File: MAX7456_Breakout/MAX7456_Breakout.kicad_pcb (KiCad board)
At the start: 4 copper layers, 18.3 x 38.6 mm, 16 parts, among them J1 Conn_01x14_Socket, U1 MAX7456EUI_, Y1 27MHz

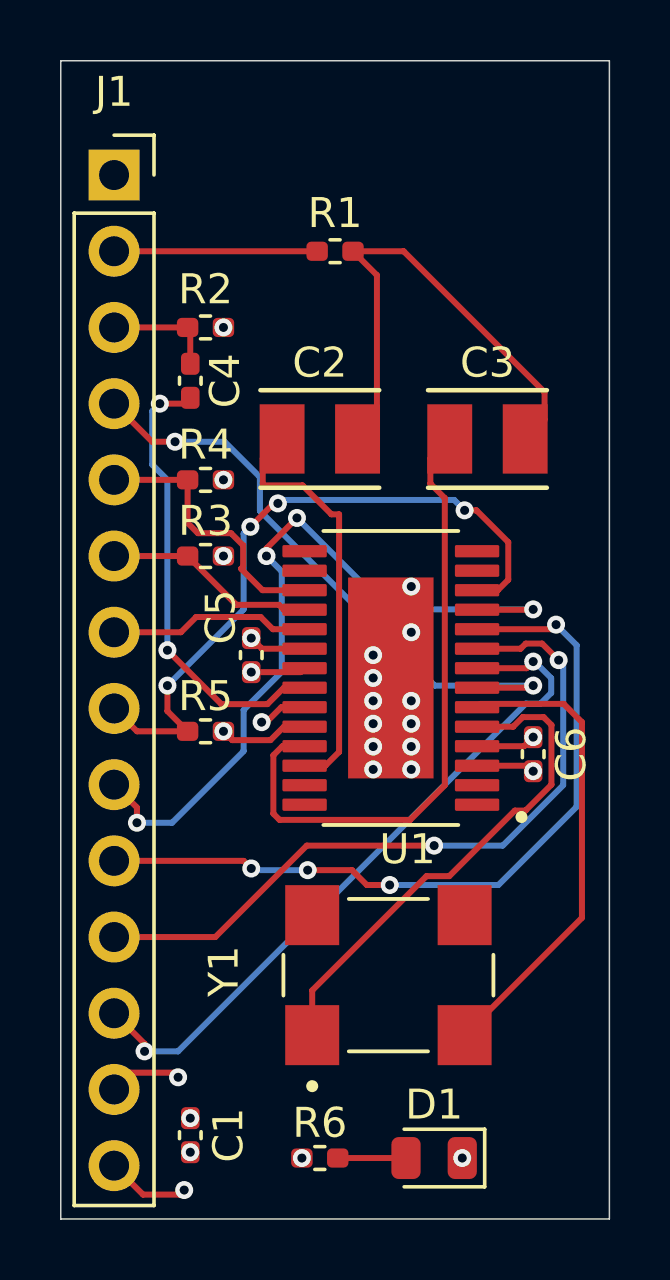
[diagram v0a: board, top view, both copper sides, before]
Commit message: Added 10k pullup on reset
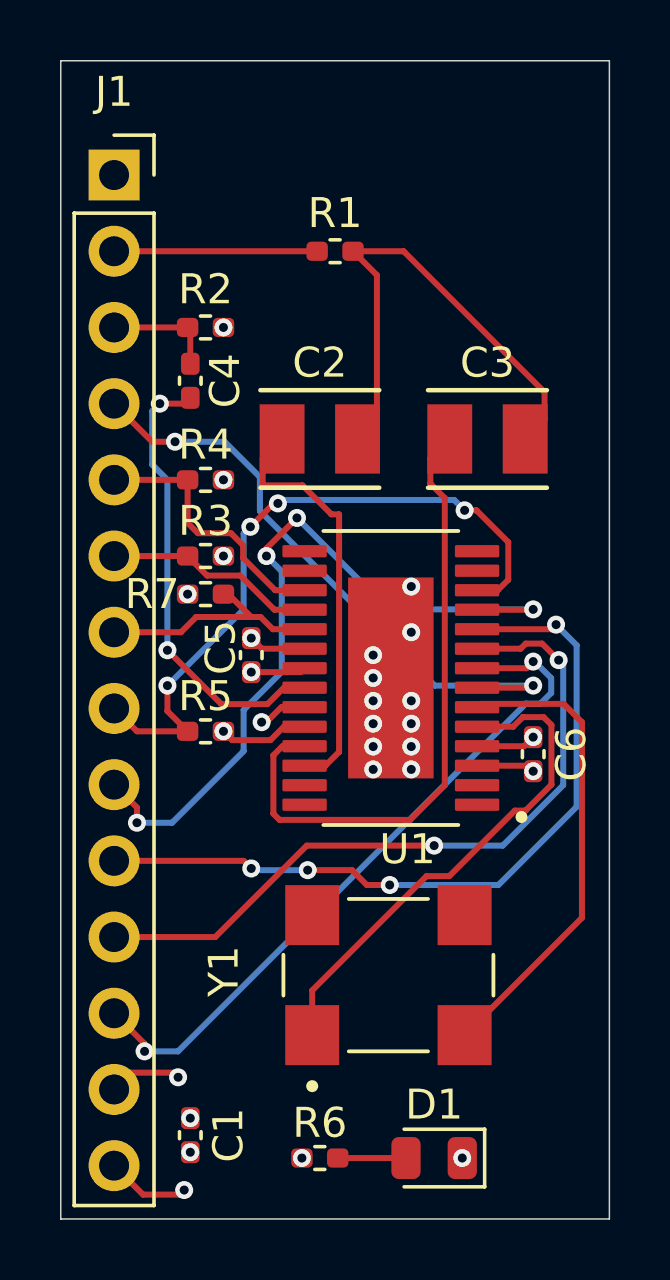
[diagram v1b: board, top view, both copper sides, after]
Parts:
- added R7: 10k, Resistor_SMD:R_0402_1005Metric_Pad0.72x0.64mm_HandSolder, F.Cu at (147.3, 97.0)
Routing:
- net RESET: track 6.73 -> 7.81 mm
- net +5V: vias 8 -> 9
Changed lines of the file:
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@@
 		(tags "capacitor handsolder")
 		(property "Reference" "C5"
-			(at 1.27 -1.016 90)
+			(at 0.254 -1.016 90)
 			(layer "F.SilkS")
 			(effects
@@
 	(footprint "Resistor_SMD:R_0402_1005Metric_Pad0.72x0.64mm_HandSolder"
 		(layer "F.Cu")
+		(at 147.32 97.028)
+		(descr "Resistor SMD 0402 (1005 Metric), square (rectangular) end terminal, IPC_7351 nominal with elongated pad for handsoldering. (Body size source: IPC-SM-782 page 72, https://www.pcb-3d.com/wordpress/wp-content/uploads/ipc-sm-782a_amendment_1_and_2.pdf), generated with kicad-footprint-generator")
+		(tags "resistor handsolder")
+		(property "Reference" "R7"
+			(at -1.778 0 0)
+			(layer "F.SilkS")
+			(effects
+				(font
+					(size 1 1)
+					(thickness 0.15)
+				)
+			)
+		)
+		(property "Value" "10k"
+			(at 0 1.17 0)
+			(layer "F.Fab")
+			(effects
+				(font
+					(size 1 1)
+					(thickness 0.15)
+				)
+			)
+		)
+		(property "Footprint" "Resistor_SMD:R_0402_1005Metric_Pad0.72x0.64mm_HandSolder"
+			(at 0 0 0)
+			(unlocked yes)
+			(layer "F.Fab")
+			(hide yes)
+			(effects
+				(font
+					(size 1.27 1.27)
+					(thickness 0.15)
+				)
+			)
+		)
+		(property "Datasheet" ""
+			(at 0 0 0)
+			(unlocked yes)
+			(layer "F.Fab")
+			(hide yes)
+			(effects
+				(font
+					(size 1.27 1.27)
+					(thickness 0.15)
+				)
+			)
+		)
+		(property "Description" "Resistor"
+			(at 0 0 0)
+			(unlocked yes)
+			(layer "F.Fab")
+			(hide yes)
+			(effects
+				(font
+					(size 1.27 1.27)
+					(thickness 0.15)
+				)
+			)
+		)
+		(property ki_fp_filters "R_*")
+		(sheetname "Root")
+		(sheetfile "MAX7456_Breakout.kicad_sch")
+		(attr smd)
+		(fp_line
+			(start -0.167621 -0.38)
+			(end 0.167621 -0.38)
+			(stroke
+				(width 0.12)
+				(type solid)
+			)
+			(layer "F.SilkS")
+		)
+		(fp_line
+			(start -0.167621 0.38)
+			(end 0.167621 0.38)
+			(stroke
+				(width 0.12)
+				(type solid)
+			)
+			(layer "F.SilkS")
+		)
+		(fp_line
+			(start -1.1 -0.47)
+			(end 1.1 -0.47)
+			(stroke
+				(width 0.05)
+				(type solid)
+			)
+			(layer "F.CrtYd")
+		)
+		(fp_line
+			(start -1.1 0.47)
+			(end -1.1 -0.47)
+			(stroke
+				(width 0.05)
+				(type solid)
+			)
+			(layer "F.CrtYd")
+		)
+		(fp_line
+			(start 1.1 -0.47)
+			(end 1.1 0.47)
+			(stroke
+				(width 0.05)
+				(type solid)
+			)
+			(layer "F.CrtYd")
+		)
+		(fp_line
+			(start 1.1 0.47)
+			(end -1.1 0.47)
+			(stroke
+				(width 0.05)
+				(type solid)
+			)
+			(layer "F.CrtYd")
+		)
+		(fp_line
+			(start -0.525 -0.27)
+			(end 0.525 -0.27)
+			(stroke
+				(width 0.1)
+				(type solid)
+			)
+			(layer "F.Fab")
+		)
+		(fp_line
+			(start -0.525 0.27)
+			(end -0.525 -0.27)
+			(stroke
+				(width 0.1)
+				(type solid)
+			)
+			(layer "F.Fab")
+		)
+		(fp_line
+			(start 0.525 -0.27)
+			(end 0.525 0.27)
+			(stroke
+				(width 0.1)
+				(type solid)
+			)
+			(layer "F.Fab")
+		)
+		(fp_line
+			(start 0.525 0.27)
+			(end -0.525 0.27)
+			(stroke
+				(width 0.1)
+				(type solid)
+			)
+			(layer "F.Fab")
+		)
+		(fp_text user "${REFERENCE}"
+			(at 0 0 0)
+			(layer "F.Fab")
+			(effects
+				(font
+					(size 0.26 0.26)
+					(thickness 0.04)
+				)
+			)
+		)
+		(pad "1" smd roundrect
+			(at -0.5975 0)
+			(size 0.715 0.64)
+			(layers "F.Cu" "F.Paste" "F.Mask")
+			(roundrect_rratio 0.25)
+			(net 1 "+5V")
+			(pintype "passive")
+		)
+		(pad "2" smd roundrect
+			(at 0.5975 0)
+			(size 0.715 0.64)
+			(layers "F.Cu" "F.Paste" "F.Mask")
+			(roundrect_rratio 0.25)
+			(net 13 "RESET")
+			(pintype "passive")
+		)
+		(model "${KICAD8_3DMODEL_DIR}/Resistor_SMD.3dshapes/R_0402_1005Metric.wrl"
+			(offset
+				(xyz 0 0 0)
+			)
+			(scale
+				(xyz 1 1 1)
+			)
+			(rotate
+				(xyz 0 0 0)
+			)
+		)
+	)
+	(footprint "Resistor_SMD:R_0402_1005Metric_Pad0.72x0.64mm_HandSolder"
+		(layer "F.Cu")
 		(at 147.32 101.6)
 		(descr "Resistor SMD 0402 (1005 Metric), square (rectangular) end terminal, IPC_7351 nominal with elongated pad for handsoldering. (Body size source: IPC-SM-782 page 72, https://www.pcb-3d.com/wordpress/wp-content/uploads/ipc-sm-782a_amendment_1_and_2.pdf), generated with kicad-footprint-generator")
@@
 	)
 	(via
+		(at 146.7225 97.028)
+		(size 0.6)
+		(drill 0.3)
+		(layers "F.Cu" "B.Cu")
+		(net 1)
+	)
+	(via
 		(at 150.5325 115.824)
 		(size 0.6)
@@
 	)
 	(segment
-		(start 148.575 96.112972)
-		(end 148.575 95.403028)
+		(start 144.272 93.218)
+		(end 146.7225 93.218)
 		(width 0.2)
 		(layer "F.Cu")
@@
 	)
 	(segment
-		(start 147.066 94.996)
-		(end 146.7225 94.6525)
+		(start 148.575 95.403028)
+		(end 148.167972 94.996)
 		(width 0.2)
 		(layer "F.Cu")
@@
 	)
 	(segment
-		(start 144.272 93.218)
+		(start 146.7225 94.6525)
 		(end 146.7225 93.218)
 		(width 0.2)
@@
 	)
 	(segment
-		(start 148.505986 96.181986)
-		(end 148.575 96.112972)
-		(width 0.2)
-		(layer "F.Cu")
-		(net 9)
-	)
-	(segment
-		(start 146.7225 94.6525)
-		(end 146.7225 93.218)
+		(start 150.622 96.897)
+		(end 149.642471 96.897)
 		(width 0.2)
 		(layer "F.Cu")
@@
 	)
 	(segment
-		(start 149.221 96.897)
-		(end 148.505986 96.181986)
+		(start 148.167972 94.996)
+		(end 147.066 94.996)
 		(width 0.2)
 		(layer "F.Cu")
@@
 	)
 	(segment
-		(start 150.622 96.897)
-		(end 149.221 96.897)
+		(start 147.066 94.996)
+		(end 146.7225 94.6525)
 		(width 0.2)
 		(layer "F.Cu")
@@
 	)
 	(segment
-		(start 148.575 95.403028)
-		(end 148.167972 94.996)
+		(start 149.642471 96.897)
+		(end 148.575 95.829529)
 		(width 0.2)
 		(layer "F.Cu")
@@
 	)
 	(segment
-		(start 148.167972 94.996)
-		(end 147.066 94.996)
+		(start 148.575 95.829529)
+		(end 148.575 95.403028)
 		(width 0.2)
 		(layer "F.Cu")
@@
 	)
 	(segment
-		(start 150.622 97.547)
-		(end 149.931336 97.547)
+		(start 148.478 96.408)
+		(end 149.617 97.547)
 		(width 0.2)
 		(layer "F.Cu")
@@
 	)
 	(segment
-		(start 149.767936 97.3836)
-		(end 148.3481 97.3836)
+		(start 149.617 97.547)
+		(end 150.622 97.547)
 		(width 0.2)
 		(layer "F.Cu")
@@
 	)
 	(segment
-		(start 149.931336 97.547)
-		(end 149.767936 97.3836)
+		(start 147.3725 96.408)
+		(end 148.478 96.408)
 		(width 0.2)
 		(layer "F.Cu")
@@
 	)
 	(segment
-		(start 148.3481 97.3836)
-		(end 146.7225 95.758)
+		(start 146.7225 95.758)
+		(end 147.3725 96.408)
 		(width 0.2)
 		(layer "F.Cu")
@@
 	)
 	(segment
-		(start 149.156762 97.79)
+		(start 150.622 98.197)
+		(end 149.563762 98.197)
+		(width 0.2)
+		(layer "F.Cu")
+		(net 13)
+	)
+	(segment
+		(start 148.844 97.79)
 		(end 147.007238 97.79)
 		(width 0.2)
@@
 	)
 	(segment
-		(start 150.622 98.197)
-		(end 149.563762 98.197)
+		(start 149.156762 97.79)
+		(end 148.844 97.79)
+		(width 0.2)
+		(layer "F.Cu")
+		(net 13)
+	)
+	(segment
+		(start 148.082 97.028)
+		(end 148.844 97.79)
 		(width 0.2)
 		(layer "F.Cu")
